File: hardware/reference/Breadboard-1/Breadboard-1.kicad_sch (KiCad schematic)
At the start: 66 parts, among them J1 Left, J2 Right, J3 ICSP, J4 Oscilloscope, J5 TTL Serial, Q31 NCE2309, Q32 NCE2309, Q33 DMN6140, Q34 DMN6140, Q35 DTC143ZCA, Q36 DTC143ZCA, Q41 2N7002, Q42 2N7002, Q43 2N7002, Q44 2N7002, Q45 2N7002, Q46 2N7002, U11 ME6203A50M3G, U21 PIC18F16Q40-I/SS

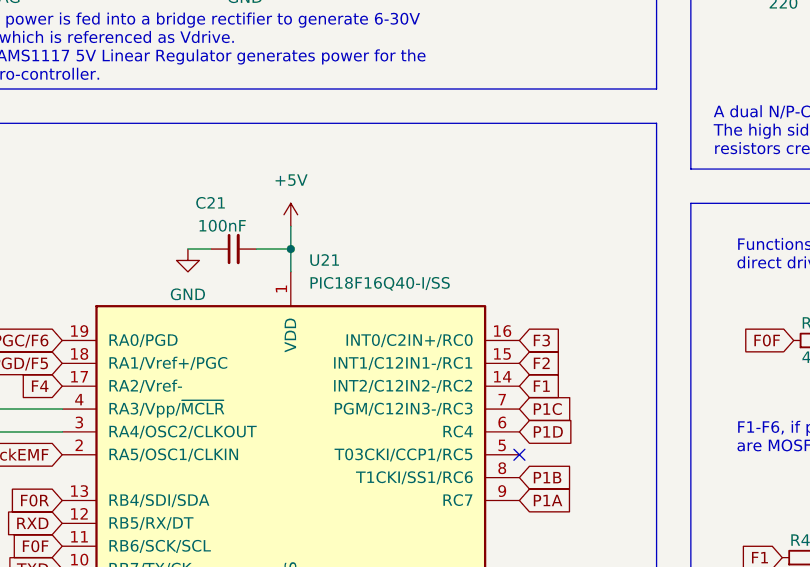
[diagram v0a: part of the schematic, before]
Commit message: Pile of minor corrections for sharing and production.
1. Remove .DS_Store files mistakenly added.
2. Correctly relatively path project footprints and symbols.
3. Add footprint for JLCPCB's required tooling hole to use their assembly service.
4. Tweak a few tracks and description placements to enhance readability.
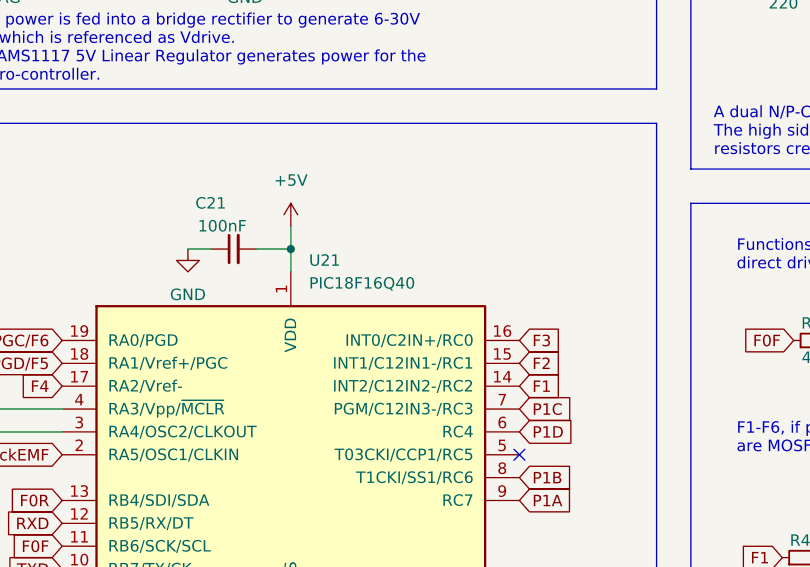
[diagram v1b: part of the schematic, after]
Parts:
- U21: value PIC18F16Q40-I/SS -> PIC18F16Q40; Specification PIC18F16Q40-I/SS, PIC18F16Q40T-I/SS, PIC18F16Q40-E/SS -> PIC18F16Q40T-I/SS, PIC18F16Q40-I/SS, PIC18F16Q40-E/SS
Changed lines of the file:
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@@
       (effects (font (size 1.27 1.27)) (justify left))
     )
-    (property "Value" "PIC18F16Q40-I/SS" (id 1) (at 75.6794 77.47 0)
+    (property "Value" "PIC18F16Q40" (id 1) (at 75.6794 77.47 0)
       (effects (font (size 1.27 1.27)) (justify left))
     )
@@
       (effects (font (size 1.27 1.27)) hide)
     )
-    (property "Specification" "PIC18F16Q40-I/SS, PIC18F16Q40T-I/SS, PIC18F16Q40-E/SS" (id 5) (at 73.66 96.52 0)
+    (property "Specification" "PIC18F16Q40T-I/SS, PIC18F16Q40-I/SS, PIC18F16Q40-E/SS" (id 5) (at 73.66 96.52 0)
       (effects (font (size 1.27 1.27)) hide)
     )
@@
     )
     (path "/204c3e6f-d2f7-4519-9db2-a96a5a61af64"
-      (reference "U21") (unit 1) (value "PIC18F16Q40-I/SS") (footprint "Package_SO:SSOP-20_5.3x7.2mm_P0.65mm")
-    )
-  )
+      (reference "U21") (unit 1) (value "PIC18F16Q40") (footprint "Package_SO:SSOP-20_5.3x7.2mm_P0.65mm")
+    )
+  )

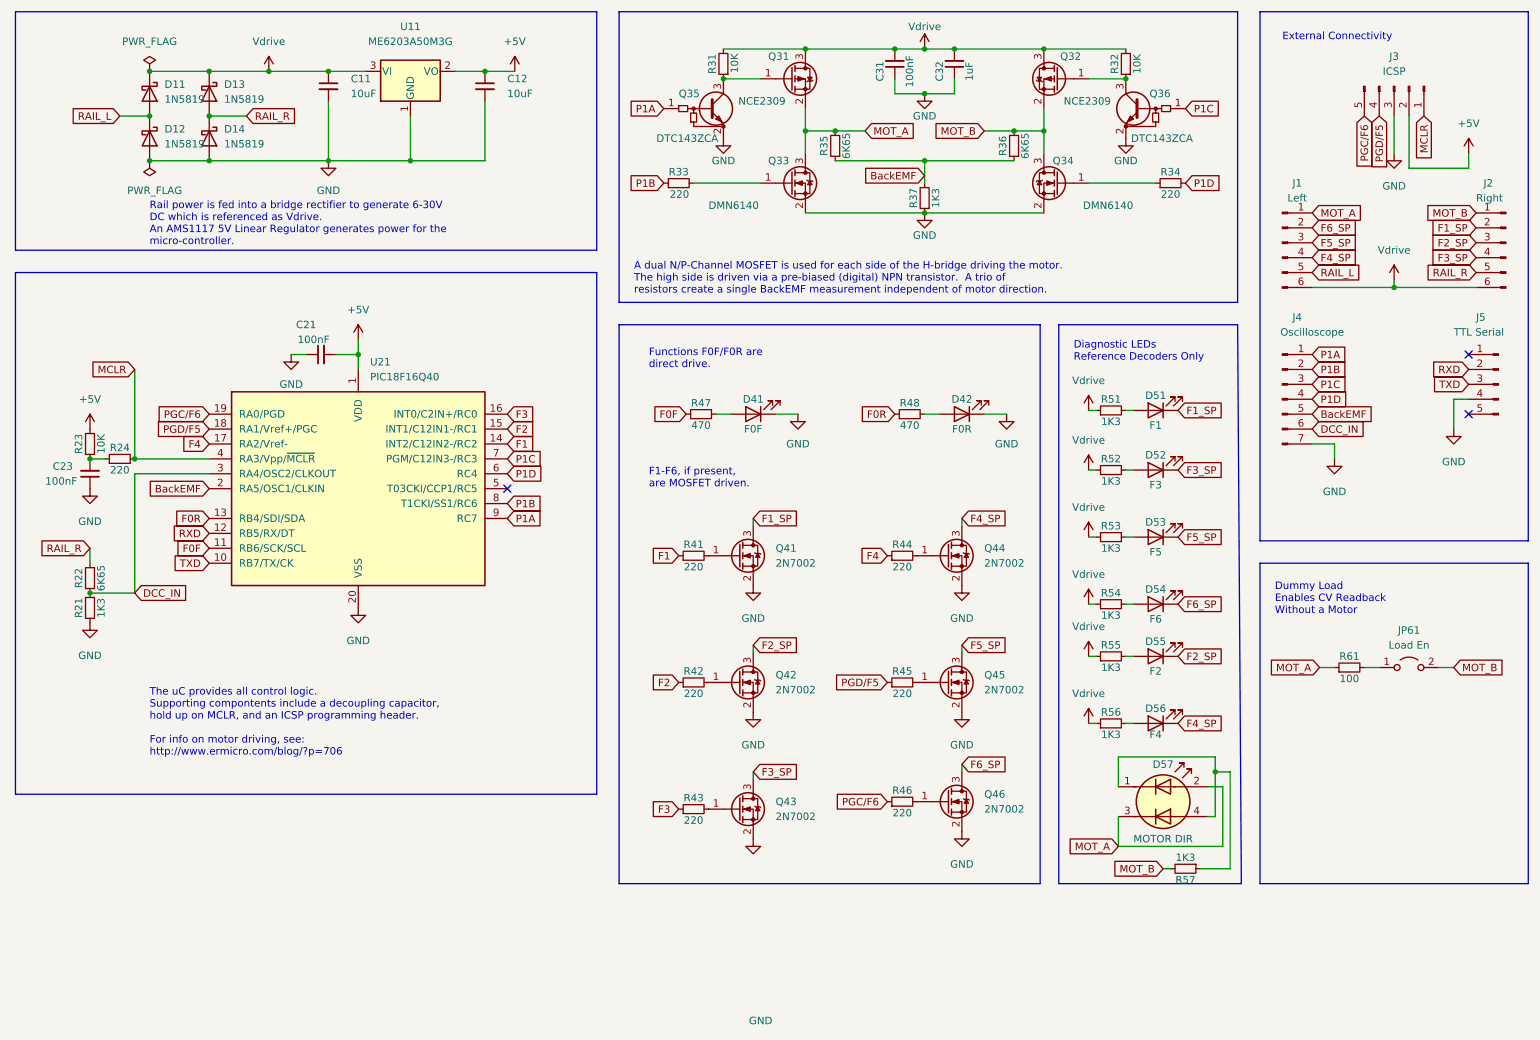
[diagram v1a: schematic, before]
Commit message: Moved CALCULATIONS to a spreadsheet.
Moved the calculations into a spreadsheet so that the values would
dynamically change when components needed to be updated.  Used the
dynamic capabilities along with the JLCPCB parts list to update
resistor values to have more common values and use JLCPCB basic
parts values.

Determined also that the calculations on the DCC input were wrong
in the previous file and added D21 to clamp the input and protect
the PIC.

Fixed the "Values" in the BOM so the components group properly.
This required also updating a number of silk screen items.

Added the copyright notice and URL to the back of the board.
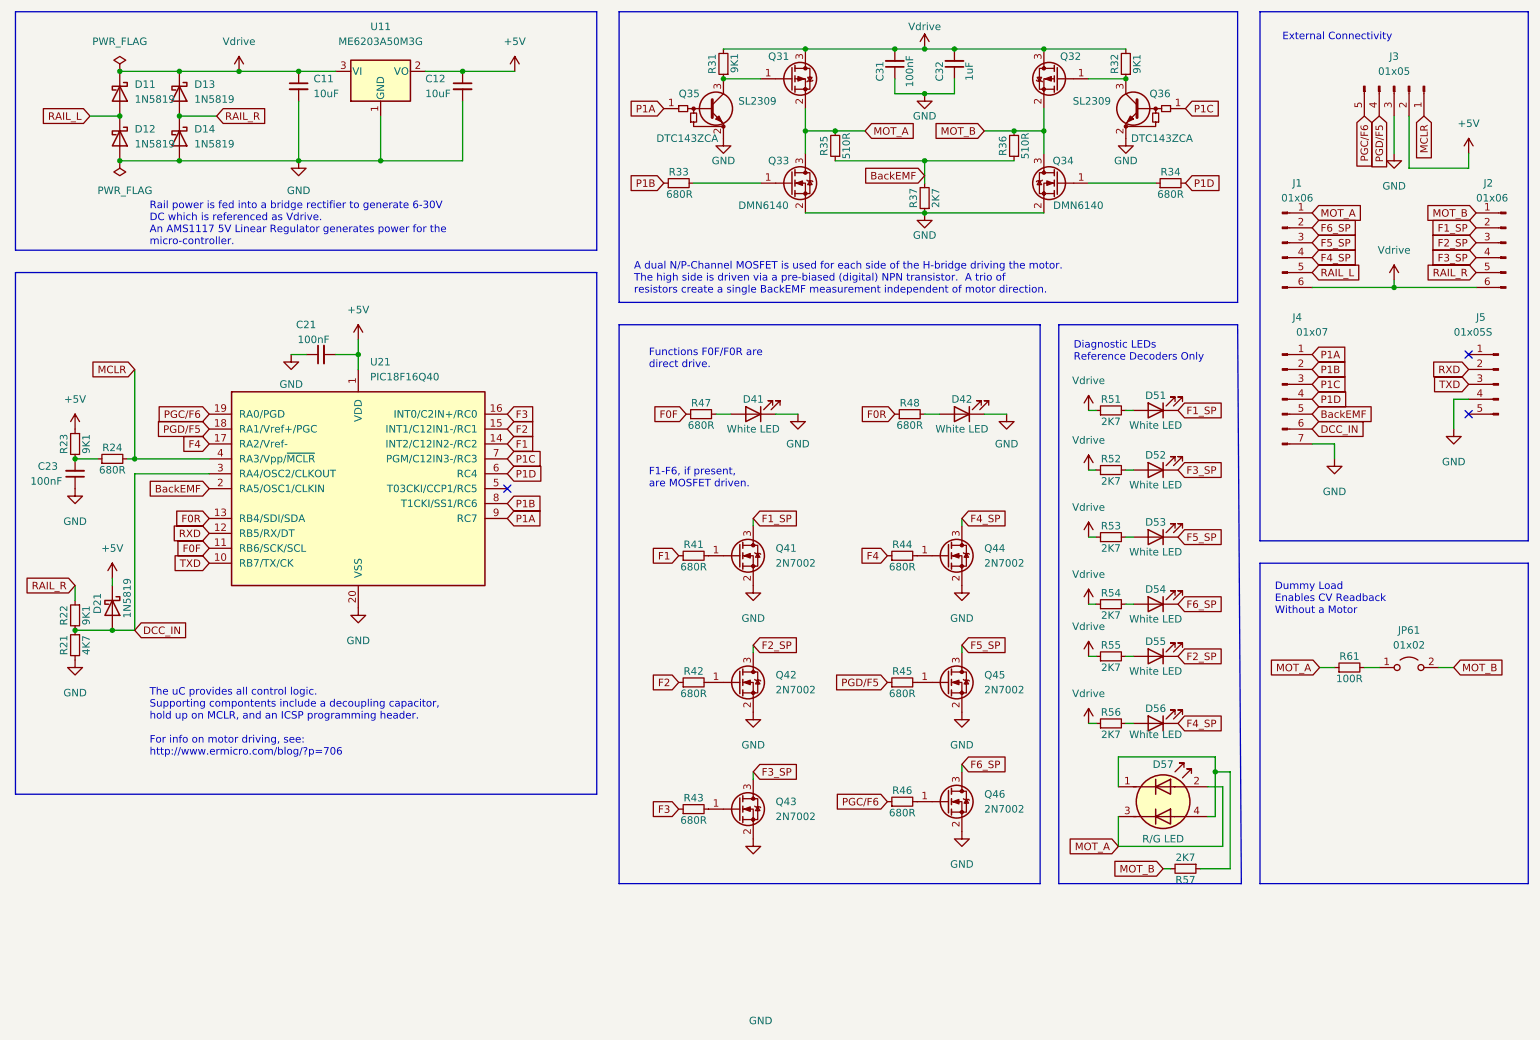
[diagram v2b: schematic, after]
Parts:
- added D21: 1N5819, Diode_SMD:D_SOD-323, symbol Device:D_Schottky
- D41: value F0F -> White LED; Cost 0.02 -> 0.01; LCSC C965818 -> C34499
- D42: value F0R -> White LED; Cost 0.02 -> 0.01; LCSC C965818 -> C34499
- D51: value F1 -> White LED; Cost 0.02 -> 0.01; LCSC C965818 -> C34499
- D52: value F3 -> White LED; Cost 0.02 -> 0.01; LCSC C965818 -> C34499
- D53: value F5 -> White LED; Cost 0.02 -> 0.01; LCSC C965818 -> C34499
- D54: value F6 -> White LED; Cost 0.02 -> 0.01; LCSC C965818 -> C34499
- D55: value F2 -> White LED; Cost 0.02 -> 0.01; LCSC C965818 -> C34499
- D56: value F4 -> White LED; Cost 0.02 -> 0.01; LCSC C965818 -> C34499
- D57: value MOTOR DIR -> R/G LED
- J1: value Left -> 01x06
- J2: value Right -> 01x06
- J3: value ICSP -> 01x05
- J4: value Oscilloscope -> 01x07
- J5: value TTL Serial -> 01x05S
- JP61: value Load En -> 01x02
- Q31, Q32: value NCE2309 -> SL2309
- R21: value 1K3 -> 4K7; LCSC C17382 -> C17673; Specification 0805 1.33K Ω 1% 1/8W -> 0805 4.7K Ω 1% 1/8W
- R22: value 6K65 -> 9K1; LCSC C17770 -> C17855; Specification 0805 6.65K Ω 1% 1/8W -> 0805 9.1K Ω 1% 1/8W
- R23, R31, R32: value 10K -> 9K1; LCSC C17414 -> C17855; Specification 0805 10K Ω 1% 1/8W -> 0805 9.1K Ω 1% 1/8W
- R24, R33, R34, R41, R42, R43, R44, R45, R46: value 220 -> 680R; LCSC C17557 -> C17798; Specification 0805 220 Ω 1% 1/8W -> 0805 680 Ω 1% 1/8W
- R35, R36: value 6K65 -> 510R; LCSC C17770 -> C17734; Specification 0805 6.65K Ω 1% 1/8W -> 0805 510 Ω 1% 1/8W
- R37, R51, R52, R53, R54, R55, R56, R57: value 1K3 -> 2K7; LCSC C17382 -> C17530; Specification 0805 1.33K Ω 1% 1/8W -> 0805 2.7K Ω 1% 1/8W
- R47, R48: value 470 -> 680R; LCSC C17710 -> C17798; Specification 0805 470 Ω 1% 1/8W -> 0805 680 Ω 1% 1/8W
- R61: value 100 -> 100R
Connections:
- net +5V: now also D21.1 (K)
- net DCC_IN: now also D21.2 (A)
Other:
- moved on the sheet: C11, C12, C23, D11, D12, D13, D14, R21, R22, R23, R24, U11

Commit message: Improved calculations, and other updates as a result.
Switched to tantalum capacitors per the data sheet recommendation
for the regulator.  Reworked board to accomodate.

Switched DCC input to be through a MOSFET to accomodate the track
voltage range.

Re-organized schematic so the blocks make more sense, changed to
US Letter paper, and re-annotated so each block has it's own 10's
range.

Updated CALCULATIONS.xlsx, including page formatting, reworked it
so there is one tab per block on the schematic, and re-checked all
calculations.  It now prints to paper pretty.

Updated all resistor values to match a 3.3v microprocessor and
JLCPCB basic parts availability.

Updated MCLR hold up circuit to include a diode to protect the rest
of the circuit while programming.

Moved the processor to the left.

Extended the board up 0.25" allowing the ICSP header to be moved
further away from the serial header.  This accomodates larger
programming adapters.

Moved the oscilloscope header up so the traces are shorter and the
board less crowded.
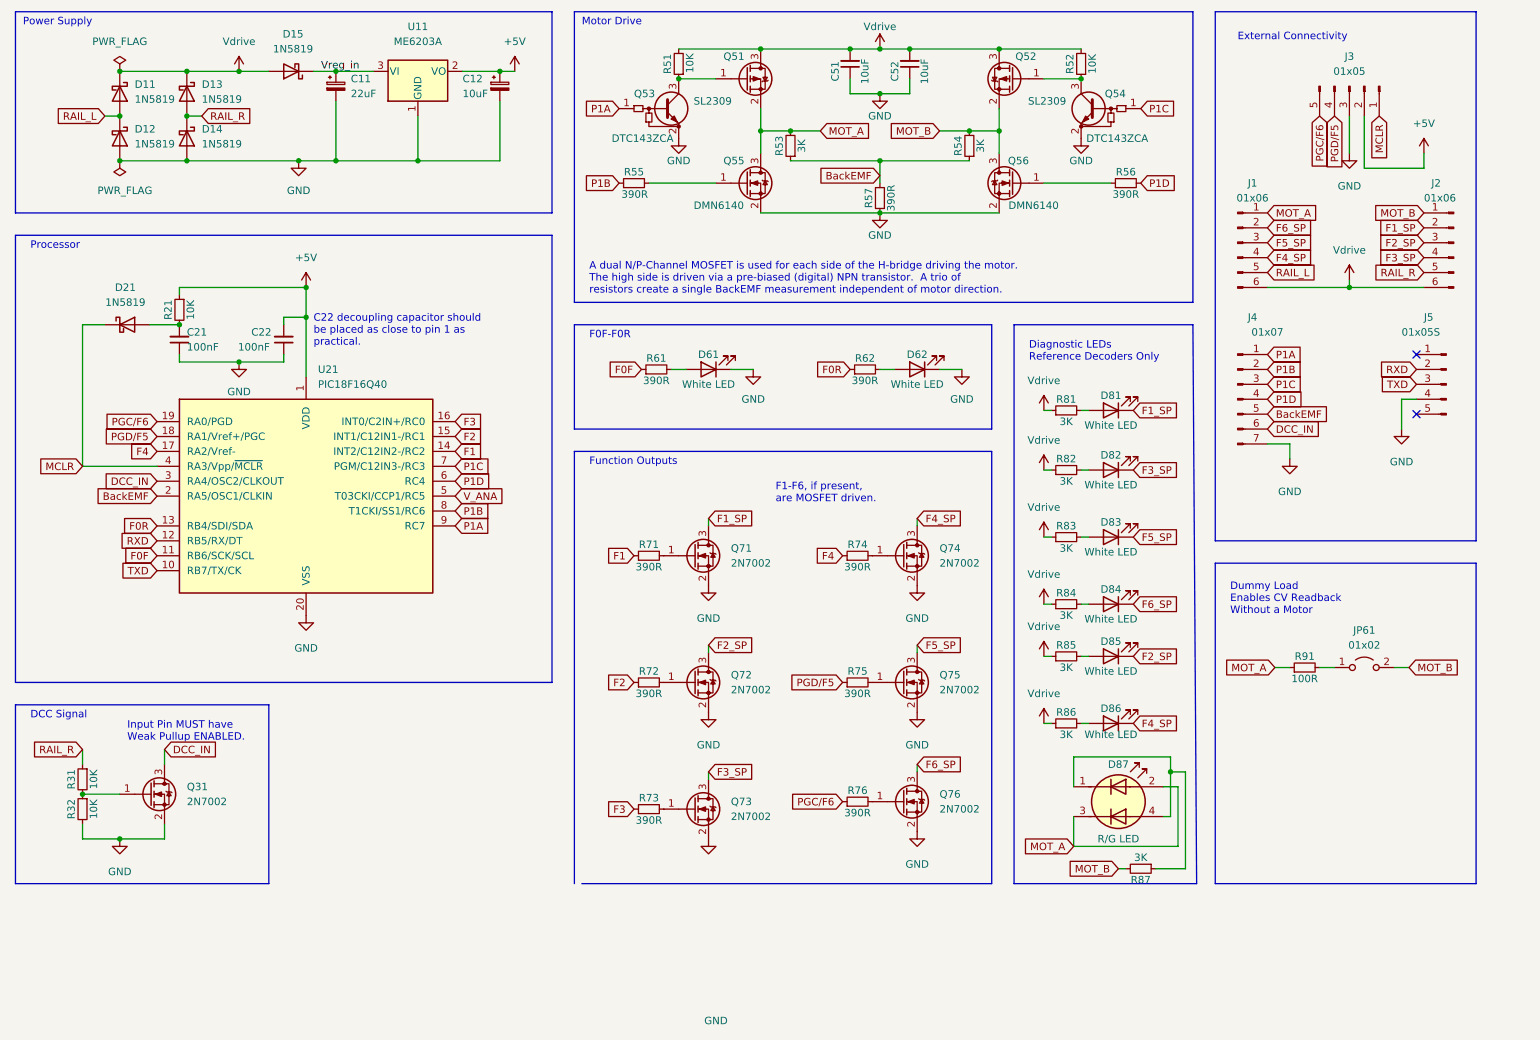
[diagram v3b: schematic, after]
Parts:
- removed R24: 680R, Resistor_SMD:R_0805_2012Metric, symbol Device:R_Small
- added D15: 1N5819, Diode_SMD:D_SOD-323, symbol Device:D_Schottky
- added Q31: 2N7002, Package_TO_SOT_SMD:SOT-23, symbol Transistor_FET:2N7002K
- C11: value 10uF -> 22uF; footprint Capacitor_SMD:C_0805_2012Metric -> Capacitor_Tantalum_SMD:CP_EIA-7343-31_Kemet-D; symbol Device:C_Small -> Device:C_Polarized_Small; Cost 0.10 -> 0.43; LCSC C440198 -> C7225; MPN (none) -> TAJD226K035RNJ; Specification 0805 50V 10uF X5R 10% -> CASE-D-7343 35V 22uF Tantalum 10%
- C12: footprint Capacitor_SMD:C_0805_2012Metric -> Capacitor_Tantalum_SMD:CP_EIA-3216-18_Kemet-A; symbol Device:C_Small -> Device:C_Polarized_Small; Cost 0.10 -> 0.09; LCSC C440198 -> C7171; MPN (none) -> TAJA106K016RNJ; Specification 0805 50V 10uF X5R 10% -> CASE-A-3216 16V 10uF Tantalum 10%
- C21: renamed from C23; MPN (none) -> Generic
- C22: renamed from C21; MPN (none) -> Generic
- C51: renamed from C31; value 100nF -> 10uF; LCSC C49678 -> C440198; MPN (none) -> Generic; Specification 0805 50V 100nF X7R 10% -> 0805 50V 10uF X5R 10%
- C52: renamed from C32; value 1uF -> 10uF; LCSC C28323 -> C440198; MPN (none) -> Generic; Specification 0805 50V 1uF X7R 10% -> 0805 50V 10uF X5R 10%
- D11, D12, D13, D14, D21: MPN (none) -> 1N5819WS
- D61: renamed from D41; MPN (none) -> KT-0805-W
- D62: renamed from D42; MPN (none) -> KT-0805-W
- D81: renamed from D51; MPN (none) -> KT-0805-W
- D82: renamed from D52; MPN (none) -> KT-0805-W
- D83: renamed from D53; MPN (none) -> KT-0805-W
- D84: renamed from D54; MPN (none) -> KT-0805-W
- D85: renamed from D55; MPN (none) -> KT-0805-W
- D86: renamed from D56; MPN (none) -> KT-0805-W
- D87: renamed from D57; MPN (none) -> XL-3227SURSYGC
- J1, J2, J3, J4, J5, JP61: MPN (none) -> DNP
- Q51: renamed from Q31; MPN (none) -> SL2309
- Q52: renamed from Q32; MPN (none) -> SL2309
- Q53: renamed from Q35; MPN (none) -> DTC143ZCA
- Q54: renamed from Q36; MPN (none) -> DTC143ZCA
- Q55: renamed from Q33; MPN (none) -> DMN6140
- Q56: renamed from Q34; MPN (none) -> DMN6140
- Q71: renamed from Q41; MPN (none) -> 2N7002
- Q72: renamed from Q42; MPN (none) -> 2N7002
- Q73: renamed from Q43; MPN (none) -> 2N7002
- Q74: renamed from Q44; MPN (none) -> 2N7002
- Q75: renamed from Q45; MPN (none) -> 2N7002
- Q76: renamed from Q46; MPN (none) -> 2N7002
- R21: renamed from R23; value 9K1 -> 10K; LCSC C17855 -> C17414; MPN (none) -> Generic; Specification 0805 9.1K Ω 1% 1/8W -> 0805 10K Ω 1% 1/8W
- R31: renamed from R22; value 9K1 -> 10K; LCSC C17855 -> C17414; MPN (none) -> Generic; Specification 0805 9.1K Ω 1% 1/8W -> 0805 10K Ω 1% 1/8W
- R32: renamed from R21; value 4K7 -> 10K; LCSC C17673 -> C17414; MPN (none) -> Generic; Specification 0805 4.7K Ω 1% 1/8W -> 0805 10K Ω 1% 1/8W
- R51: renamed from R31; value 9K1 -> 10K; LCSC C17855 -> C17414; MPN (none) -> Generic; Specification 0805 9.1K Ω 1% 1/8W -> 0805 10K Ω 1% 1/8W
- R52: renamed from R32; value 9K1 -> 10K; LCSC C17855 -> C17414; MPN (none) -> Generic; Specification 0805 9.1K Ω 1% 1/8W -> 0805 10K Ω 1% 1/8W
- R53: renamed from R35; value 510R -> 3K; LCSC C17734 -> C17661; MPN (none) -> Generic; Specification 0805 510 Ω 1% 1/8W -> 0805 3K Ω 1% 1/8W
- R54: renamed from R36; value 510R -> 3K; LCSC C17734 -> C17661; MPN (none) -> Generic; Specification 0805 510 Ω 1% 1/8W -> 0805 3K Ω 1% 1/8W
- R55: renamed from R33; value 680R -> 390R; LCSC C17798 -> C17655; MPN (none) -> Generic; Specification 0805 680 Ω 1% 1/8W -> 0805 390 Ω 1% 1/8W
- R56: renamed from R34; value 680R -> 390R; LCSC C17798 -> C17655; MPN (none) -> Generic; Specification 0805 680 Ω 1% 1/8W -> 0805 390 Ω 1% 1/8W
- R57: renamed from R37; value 2K7 -> 390R; LCSC C17530 -> C17655; MPN (none) -> Generic; Specification 0805 2.7K Ω 1% 1/8W -> 0805 390 Ω 1% 1/8W
- R61: renamed from R47; value 680R -> 390R; LCSC C17798 -> C17655; MPN (none) -> Generic; Specification 0805 680 Ω 1% 1/8W -> 0805 390 Ω 1% 1/8W
- R62: renamed from R48; value 680R -> 390R; LCSC C17798 -> C17655; MPN (none) -> Generic; Specification 0805 680 Ω 1% 1/8W -> 0805 390 Ω 1% 1/8W
- R71: renamed from R41; value 680R -> 390R; LCSC C17798 -> C17655; MPN (none) -> Generic; Specification 0805 680 Ω 1% 1/8W -> 0805 390 Ω 1% 1/8W
- R72: renamed from R42; value 680R -> 390R; LCSC C17798 -> C17655; MPN (none) -> Generic; Specification 0805 680 Ω 1% 1/8W -> 0805 390 Ω 1% 1/8W
- R73: renamed from R43; value 680R -> 390R; LCSC C17798 -> C17655; MPN (none) -> Generic; Specification 0805 680 Ω 1% 1/8W -> 0805 390 Ω 1% 1/8W
- R74: renamed from R44; value 680R -> 390R; LCSC C17798 -> C17655; MPN (none) -> Generic; Specification 0805 680 Ω 1% 1/8W -> 0805 390 Ω 1% 1/8W
- R75: renamed from R45; value 680R -> 390R; LCSC C17798 -> C17655; MPN (none) -> Generic; Specification 0805 680 Ω 1% 1/8W -> 0805 390 Ω 1% 1/8W
- R76: renamed from R46; value 680R -> 390R; LCSC C17798 -> C17655; MPN (none) -> Generic; Specification 0805 680 Ω 1% 1/8W -> 0805 390 Ω 1% 1/8W
- R81: renamed from R51; value 2K7 -> 3K; LCSC C17530 -> C17661; MPN (none) -> Generic; Specification 0805 2.7K Ω 1% 1/8W -> 0805 3K Ω 1% 1/8W
- R82: renamed from R52; value 2K7 -> 3K; LCSC C17530 -> C17661; MPN (none) -> Generic; Specification 0805 2.7K Ω 1% 1/8W -> 0805 3K Ω 1% 1/8W
- R83: renamed from R53; value 2K7 -> 3K; LCSC C17530 -> C17661; MPN (none) -> Generic; Specification 0805 2.7K Ω 1% 1/8W -> 0805 3K Ω 1% 1/8W
- R84: renamed from R54; value 2K7 -> 3K; LCSC C17530 -> C17661; MPN (none) -> Generic; Specification 0805 2.7K Ω 1% 1/8W -> 0805 3K Ω 1% 1/8W
- R85: renamed from R55; value 2K7 -> 3K; LCSC C17530 -> C17661; MPN (none) -> Generic; Specification 0805 2.7K Ω 1% 1/8W -> 0805 3K Ω 1% 1/8W
- R86: renamed from R56; value 2K7 -> 3K; LCSC C17530 -> C17661; MPN (none) -> Generic; Specification 0805 2.7K Ω 1% 1/8W -> 0805 3K Ω 1% 1/8W
- R87: renamed from R57; value 2K7 -> 3K; LCSC C17530 -> C17661; MPN (none) -> Generic; Specification 0805 2.7K Ω 1% 1/8W -> 0805 3K Ω 1% 1/8W
- R91: renamed from R61; MPN (none) -> RC2512JK-7W100RL
- U11: value ME6203A50M3G -> ME6203A; LCSC C92717 -> C87842; MPN (none) -> ME6203A33M3G; Specification SOT-23 180ma 40V to 5V LDO -> SOT-23 100ma 40V to 3.3V LDO
- U21: MPN (none) -> PIC18F16Q40T-I/SS
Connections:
- net +5V: no longer D21.1 (K)
- net DCC_IN: now also Q31.3 (D); no longer D21.2 (A), R31.2, R32.1
- net GND: now also Q31.2 (S)
- net MCLR: now also D21.1 (K)
- net Vdrive: now also D15.2 (A); no longer C11.1, U11.3 (VI)
- net at C21.2, R21.2: now also D21.2 (A)
- net V_ANA: now reaches U21.5 (T03CKI/CCP1/RC5)
- new net: Q31.1 (G), R31.2, R32.1
- new net Vreg_in: C11.1, D15.1 (K), U11.3 (VI)
- no-connect marks 3 -> 2
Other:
- note added: "C22 decoupling capacitor should be placed as close to pin 1 as practical."
- note added: "DCC Signal"
- note added: "F0F-F0R"
- note added: "Function Outputs"
- note added: "Input Pin MUST have Weak Pullup ENABLED."
- note added: "Motor Drive"
- note added: "Power Supply"
- note added: "Processor"
- note removed: "Functions F0F/F0R are direct drive."
- note removed: "Rail power is fed into a bridge rectifier to generate 6-30V DC which is referenced as Vdrive. An AMS1117 5V Linear Regulator generates power for the micro-controller."
- note removed: "The uC provides all control logic. Supporting compontents include a decoupling capacitor, hold up on MCLR, and an ICSP programming header. For info on motor driving, see: http://www.ermicro.com/blog/?p=706"
- company: (none) -> https://github.com/bicknell/DCC-Mobile-Decoder
- title: (none) -> Breadboard-1
- moved on the sheet: C21, C22, C51, C52, D13, D14, D61, D62, D81, D82, D83, D84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
